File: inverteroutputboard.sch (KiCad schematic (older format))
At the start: 111 parts, among them P1 B+, P2 finishwinding, P3 B+, P4 startwinding, P5 CONN_02X05, Q1 Q_NMOS_GDS, Q10 Q_NMOS_GDS, Q11 Q_NMOS_GDS, Q12 Q_NMOS_GDS, Q13 Q_NMOS_GDS, Q14 Q_NMOS_GDS, Q15 Q_NMOS_GDS, Q16 Q_NMOS_GDS, Q17 Q_NMOS_GDS, Q18 Q_NMOS_GDS, Q19 Q_NMOS_GDS, Q2 Q_NMOS_GDS, Q20 Q_NMOS_GDS, Q21 Q_NMOS_GDS, Q22 Q_NMOS_GDS, Q23 Q_NMOS_GDS, Q24 Q_NMOS_GDS, Q3 Q_NMOS_GDS, Q4 Q_NMOS_GDS, Q5 Q_NMOS_GDS, Q6 Q_NMOS_GDS, Q7 Q_NMOS_GDS, Q8 Q_NMOS_GDS, Q9 Q_NMOS_GDS

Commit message: added jumbpers
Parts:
- removed C2, C4, C5: 104/100v, Capacitors_ThroughHole:C_Disc_D7.5_P5, symbol C
- removed C3, C6: 472/1kv, Capacitors_ThroughHole:C_Disc_D12_P7.75, symbol C
- removed D10, D11, D12, D13, D14, D15, D16, D17, D19, D20, D21, D22, D23, D24, D7, D8, D9: 1N5819, Diodes_SMD:DO-214AB_Handsoldering, symbol D_Schottky_Small
- removed D18: D_Schottky_Small, Diodes_SMD:DO-214AB_Handsoldering, symbol D_Schottky_Small
- removed P2: finishwinding, Connect:1pin, symbol CONN_01X01
- removed P3: B+, Connect:1pin, symbol CONN_01X01
- removed P4: startwinding, Connect:1pin, symbol CONN_01X01
- removed Q10, Q11, Q12, Q13, Q14, Q15, Q16, Q17, Q18, Q19, Q20, Q21, Q22, Q23, Q24, Q7, Q8, Q9: Q_NMOS_GDS, TO_SOT_Packages_THT:TO-220_Neutral123_Horizontal_MountedFromLS_LargePads, symbol Q_NMOS_GDS
- removed R14, R27, R40: 47R1/2w, Resistors_ThroughHole:Resistor_Horizontal_RM10mm, symbol R
- removed R15, R16, R18, R19, R20, R21, R28, R29, R31, R32, R33, R34, R41, R42, R44, R45, R46, R47: 20k, Resistors_SMD:R_0603_HandSoldering, symbol R
- removed R17, R22, R23, R24, R25, R26, R30, R35, R36, R37, R38, R39, R43, R48, R49, R50, R51, R52: 5.6, Resistors_SMD:R_0603_HandSoldering, symbol R
- added JP?: pwm-c, symbol JUMPER
- added JP?: pwm-d, symbol JUMPER
- added JP?: pwm-b, symbol JUMPER
- added JP?: pwm-a, symbol JUMPER
- added JP?: endwind, symbol JUMPER
- added JP?: startwind, symbol JUMPER
- added JP?: gnd, symbol JUMPER
- added JP?: b+, symbol JUMPER
- added P?: CONN_02X05, Connect:IDC_Header_Straight_10pins, symbol CONN_02X05
- Q1, Q2, Q3, Q4, Q5, Q6: footprint TO_SOT_Packages_THT:TO-220_Neutral123_Horizontal_MountedFromLS_LargePads -> TO_SOT_Packages_THT:TO-220_Neutral123_Vertical
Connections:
- net B+: now also JP?.1, JP?.2, P?.10 (P10), P?.9 (P9)
- net GND: now also JP?.1, P?.1 (P1), P?.2 (P2)
- net PWM-A: now also JP?.1, P?.3 (P3)
- net PWM-B: now also JP?.1, P?.7 (P7)
- net PWM-C: now also D3.1 (K), JP?.1, JP?.2, JP?.2, JP?.2, JP?.2, P?.4 (P4)
- net PWM-D: now also JP?.1, P?.8 (P8)
- net endwinding: now also JP?.1, JP?.2, JP?.2, JP?.2, P?.6 (P6)
- net startwinding: now also JP?.1, P?.5 (P5)
- net at Q4.1 (G), R12.1, R8.1: now also D3.2 (A)
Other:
- moved on the sheet: P5

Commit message: version 0.9 caps and connectors
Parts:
- removed P1: B+, Connect:1pin, symbol CONN_01X01
- added C2, C3: CP, Capacitors_ThroughHole:C_Radial_D35_L51_P10, symbol CP
- JP1, JP2, JP3, JP4, JP5, JP6, JP7, JP8: renamed from JP?; footprint (none) -> Connectors_JST:JST_EH_B02B-EH-A_02x2.50mm_Straight
- gave numbers to parts that had none: 1
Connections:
- net B+: no longer C1.2, JP1.2, Q1.2 (D), Q2.2 (D), Q3.2 (D), Q4.2 (D), Q5.2 (D), Q6.2 (D)
- net PWM-C: no longer D1.1 (K), D2.1 (K), D3.1 (K), D4.1 (K), D5.1 (K), D6.1 (K), JP2.2, JP3.2, JP4.2, JP5.2, R10.2, R11.2, R12.2, R13.2, R4.2, R9.2
- net endwinding: no longer JP6.2, JP7.2, JP8.2, Q1.3 (S), Q2.3 (S), Q3.3 (S), Q4.3 (S), Q5.3 (S), Q6.3 (S), R1.2, R2.2, R3.2, R5.2, R6.2, R7.2, R8.2
- new net: C1.2, JP1.2, Q1.2 (D), Q2.2 (D), Q3.2 (D), Q4.2 (D), Q5.2 (D), Q6.2 (D)
- new net: JP6.2, JP7.2, JP8.2, Q1.3 (S), Q2.3 (S), Q3.3 (S), Q4.3 (S), Q5.3 (S), Q6.3 (S), R1.2, R2.2, R3.2, R5.2, R6.2, R7.2, R8.2
- new net: D1.1 (K), D2.1 (K), D3.1 (K), D4.1 (K), D5.1 (K), D6.1 (K), JP2.2, JP3.2, JP4.2, JP5.2, R10.2, R11.2, R12.2, R13.2, R4.2, R9.2
- new net: C2.1, C3.1
- new net: C2.2, C3.2
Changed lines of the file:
@@
 	7950 1500 7950 1475
 Connection ~ 4200 1750
-$Comp
-L CONN_01X01 P1
-U 1 1 57CCC886
-P 3175 1075
-F 0 "P1" H 3175 1175 50  0000 C CNN
-F 1 "B+" V 3275 1075 50  0000 C CNN
-F 2 "Connect:1pin" H 3175 1075 50  0001 C CNN
-F 3 "" H 3175 1075 50  0000 C CNN
-	1    3175 1075
-	-1   0    0    1
-$EndComp
 Wire Wire Line
 	3375 1075 4250 1075
@@
 	4250 1075 4250 1150
 Connection ~ 4250 1150
-Text Label 3175 1875 0    60   ~ 0
-PWM-C
 Wire Wire Line
 	3175 1875 3600 1875
 Connection ~ 3600 1875
-Text Label 3725 975  0    60   ~ 0
-B+
 Wire Wire Line
 	3725 975  3725 1075
@@
 	7475 1850 7475 1900
 Connection ~ 7475 1900
-Text Label 4000 1750 0    60   ~ 0
-endwinding
 Wire Wire Line
 	5375 1650 5375 1525
@@
 Connection ~ 5375 1900
 $Comp
-L CONN_02X05 P?
+L CONN_02X05 P2
 U 1 1 58034A1E
 P 2300 4975
-F 0 "P?" H 2300 5275 50  0000 C CNN
+F 0 "P2" H 2300 5275 50  0000 C CNN
 F 1 "CONN_02X05" H 2300 4675 50  0000 C CNN
 F 2 "Connect:IDC_Header_Straight_10pins" H 2300 3775 50  0001 C CNN
@@
 Connection ~ 2275 4575
 $Comp
-L GND #PWR?
+L GND #PWR02
 U 1 1 58034A2B
 P 2300 5425
-F 0 "#PWR?" H 2300 5175 50  0001 C CNN
+F 0 "#PWR02" H 2300 5175 50  0001 C CNN
 F 1 "GND" H 2300 5275 50  0000 C CNN
 F 2 "" H 2300 5425 50  0000 C CNN
@@
 	1950 4875 2050 4875
 $Comp
-L JUMPER JP?
+L JUMPER JP5
 U 1 1 58034C90
 P 2850 1875
-F 0 "JP?" H 2850 2025 50  0000 C CNN
+F 0 "JP5" H 2850 2025 50  0000 C CNN
 F 1 "pwm-c" H 2850 1795 50  0000 C CNN
-F 2 "" H 2850 1875 50  0000 C CNN
+F 2 "Connectors_JST:JST_EH_B02B-EH-A_02x2.50mm_Straight" H 2850 1875 50  0001 C CNN
 F 3 "" H 2850 1875 50  0000 C CNN
 	1    2850 1875
@@
 $EndComp
 $Comp
-L JUMPER JP?
+L JUMPER JP3
 U 1 1 58034D23
 P 2825 1625
-F 0 "JP?" H 2825 1775 50  0000 C CNN
+F 0 "JP3" H 2825 1775 50  0000 C CNN
 F 1 "pwm-d" H 2825 1545 50  0000 C CNN
-F 2 "" H 2825 1625 50  0000 C CNN
+F 2 "Connectors_JST:JST_EH_B02B-EH-A_02x2.50mm_Straight" H 2825 1625 50  0001 C CNN
 F 3 "" H 2825 1625 50  0000 C CNN
 	1    2825 1625
@@
 $EndComp
 $Comp
-L JUMPER JP?
+L JUMPER JP2
 U 1 1 58034DAC
 P 2825 1350
-F 0 "JP?" H 2825 1500 50  0000 C CNN
+F 0 "JP2" H 2825 1500 50  0000 C CNN
 F 1 "pwm-b" H 2825 1270 50  0000 C CNN
-F 2 "" H 2825 1350 50  0000 C CNN
+F 2 "Connectors_JST:JST_EH_B02B-EH-A_02x2.50mm_Straight" H 2825 1350 50  0001 C CNN
 F 3 "" H 2825 1350 50  0000 C CNN
 	1    2825 1350
@@
 $EndComp
 $Comp
-L JUMPER JP?
+L JUMPER JP4
 U 1 1 58034E3E
 P 2825 2075
-F 0 "JP?" H 2825 2225 50  0000 C CNN
+F 0 "JP4" H 2825 2225 50  0000 C CNN
 F 1 "pwm-a" H 2825 1995 50  0000 C CNN
-F 2 "" H 2825 2075 50  0000 C CNN
+F 2 "Connectors_JST:JST_EH_B02B-EH-A_02x2.50mm_Straight" H 2825 2075 50  0001 C CNN
 F 3 "" H 2825 2075 50  0000 C CNN
 	1    2825 2075
@@
 	2525 2025 2525 2075
 $Comp
-L JUMPER JP?
+L JUMPER JP7
 U 1 1 58035E03
 P 4100 2250
-F 0 "JP?" H 4100 2400 50  0000 C CNN
+F 0 "JP7" H 4100 2400 50  0000 C CNN
 F 1 "endwind" H 4100 2170 50  0000 C CNN
-F 2 "" H 4100 2250 50  0000 C CNN
+F 2 "Connectors_JST:JST_EH_B02B-EH-A_02x2.50mm_Straight" H 4100 2250 50  0001 C CNN
 F 3 "" H 4100 2250 50  0000 C CNN
 	1    4100 2250
@@
 Connection ~ 4400 1750
 $Comp
-L JUMPER JP?
+L JUMPER JP6
 U 1 1 58035F8A
 P 4075 2500
-F 0 "JP?" H 4075 2650 50  0000 C CNN
+F 0 "JP6" H 4075 2650 50  0000 C CNN
 F 1 "startwind" H 4075 2420 50  0000 C CNN
-F 2 "" H 4075 2500 50  0000 C CNN
+F 2 "Connectors_JST:JST_EH_B02B-EH-A_02x2.50mm_Straight" H 4075 2500 50  0001 C CNN
 F 3 "" H 4075 2500 50  0000 C CNN
 	1    4075 2500
@@
 Connection ~ 2800 2775
 $Comp
-L JUMPER JP?
+L JUMPER JP8
 U 1 1 580368FD
 P 4100 2950
-F 0 "JP?" H 4100 3100 50  0000 C CNN
+F 0 "JP8" H 4100 3100 50  0000 C CNN
 F 1 "gnd" H 4100 2870 50  0000 C CNN
-F 2 "" H 4100 2950 50  0000 C CNN
+F 2 "Connectors_JST:JST_EH_B02B-EH-A_02x2.50mm_Straight" H 4100 2950 50  0001 C CNN
 F 3 "" H 4100 2950 50  0000 C CNN
 	1    4100 2950
@@
 Connection ~ 2625 3050
 $Comp
-L JUMPER JP?
+L JUMPER JP1
 U 1 1 58037102
 P 2725 800
-F 0 "JP?" H 2725 950 50  0000 C CNN
+F 0 "JP1" H 2725 950 50  0000 C CNN
 F 1 "b+" H 2725 720 50  0000 C CNN
-F 2 "" H 2725 800 50  0000 C CNN
+F 2 "Connectors_JST:JST_EH_B02B-EH-A_02x2.50mm_Straight" H 2725 800 50  0001 C CNN
 F 3 "" H 2725 800 50  0000 C CNN
 	1    2725 800
@@
 Wire Wire Line
 	2425 700  2425 800
+Connection ~ 3175 1875
+$Comp
+L CP C2
+U 1 1 5803BE58
+P 5225 3850
+F 0 "C2" H 5250 3950 50  0000 L CNN
+F 1 "CP" H 5250 3750 50  0000 L CNN
+F 2 "Capacitors_ThroughHole:C_Radial_D35_L51_P10" H 5263 3700 50  0001 C CNN
+F 3 "" H 5225 3850 50  0000 C CNN
+	1    5225 3850
+	1    0    0    -1
+$EndComp
+$Comp
+L CP C3
+U 1 1 5803BF11
+P 5600 3875
+F 0 "C3" H 5625 3975 50  0000 L CNN
+F 1 "CP" H 5625 3775 50  0000 L CNN
+F 2 "Capacitors_ThroughHole:C_Radial_D35_L51_P10" H 5638 3725 50  0001 C CNN
+F 3 "" H 5600 3875 50  0000 C CNN
+	1    5600 3875
+	1    0    0    -1
+$EndComp
+Wire Wire Line
+	5225 3700 5600 3700
+Wire Wire Line
+	5600 3700 5600 3725
+Wire Wire Line
+	5600 4025 5225 4025
+Wire Wire Line
+	5225 4025 5225 4000
 $EndSCHEMATC

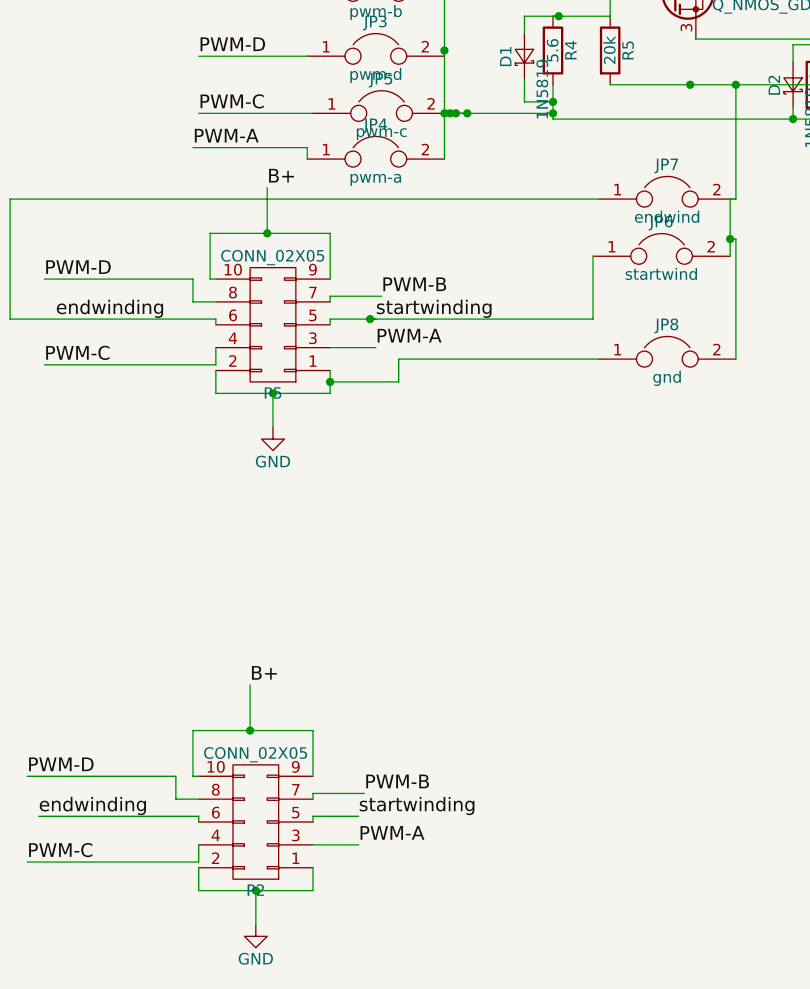
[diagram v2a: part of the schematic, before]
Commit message: reworked plugs to make compatible with powerstar inverters and added better solder masking.
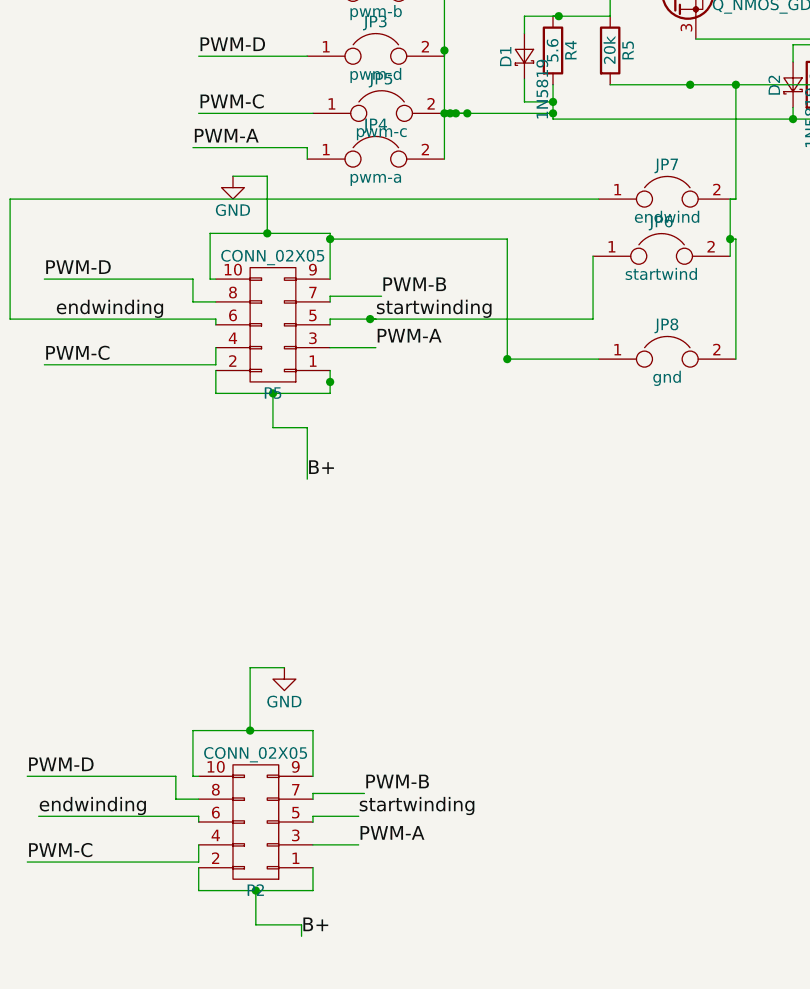
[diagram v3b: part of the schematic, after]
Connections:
- net B+: now also P2.1 (P1), P2.2 (P2), P5.1 (P1), P5.2 (P2); no longer P2.10 (P10), P2.9 (P9), P5.10 (P10), P5.9 (P9)
- net GND: now also P2.10 (P10), P2.9 (P9), P5.10 (P10), P5.9 (P9); no longer P2.1 (P1), P2.2 (P2), P5.1 (P1), P5.2 (P2)
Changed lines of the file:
@@
 Wire Wire Line
 	2625 2400 2625 2600
-Text Label 2350 2200 0    60   ~ 0
+Text Label 2525 3475 0    60   ~ 0
 B+
 Wire Wire Line
-	2350 2200 2350 2400
+	2350 2150 2350 2400
 Connection ~ 2350 2400
 $Comp
 L GND #PWR01
 U 1 1 57CD0DDC
-P 2375 3250
-F 0 "#PWR01" H 2375 3000 50  0001 C CNN
-F 1 "GND" H 2375 3100 50  0000 C CNN
-F 2 "" H 2375 3250 50  0000 C CNN
-F 3 "" H 2375 3250 50  0000 C CNN
-	1    2375 3250
+P 2200 2150
+F 0 "#PWR01" H 2200 1900 50  0001 C CNN
+F 1 "GND" H 2200 2000 50  0000 C CNN
+F 2 "" H 2200 2150 50  0000 C CNN
+F 3 "" H 2200 2150 50  0000 C CNN
+	1    2200 2150
 	1    0    0    -1
 $EndComp
@@
 Wire Wire Line
 	2550 4575 2550 4775
-Text Label 2275 4375 0    60   ~ 0
+Text Label 2500 5475 0    60   ~ 0
 B+
 Wire Wire Line
-	2275 4375 2275 4575
+	2275 4300 2275 4575
 Connection ~ 2275 4575
 $Comp
 L GND #PWR02
 U 1 1 58034A2B
-P 2300 5425
-F 0 "#PWR02" H 2300 5175 50  0001 C CNN
-F 1 "GND" H 2300 5275 50  0000 C CNN
-F 2 "" H 2300 5425 50  0000 C CNN
-F 3 "" H 2300 5425 50  0000 C CNN
-	1    2300 5425
+P 2425 4300
+F 0 "#PWR02" H 2425 4050 50  0001 C CNN
+F 1 "GND" H 2425 4150 50  0000 C CNN
+F 2 "" H 2425 4300 50  0000 C CNN
+F 3 "" H 2425 4300 50  0000 C CNN
+	1    2425 4300
 	1    0    0    -1
 $EndComp
@@
 	4400 2425 4375 2425
 Connection ~ 4375 2425
-Wire Wire Line
-	3800 2950 2925 2950
-Wire Wire Line
-	2925 2950 2925 3050
-Wire Wire Line
-	2925 3050 2625 3050
 Connection ~ 2625 3050
 $Comp
@@
 Wire Wire Line
 	5225 4025 5225 4000
+Wire Wire Line
+	2275 4300 2425 4300
+Wire Wire Line
+	2300 5425 2500 5425
+Wire Wire Line
+	2500 5425 2500 5475
+Wire Wire Line
+	2200 2150 2350 2150
+Wire Wire Line
+	2375 3250 2525 3250
+Wire Wire Line
+	2525 3250 2525 3475
+Wire Wire Line
+	2625 2425 3400 2425
+Wire Wire Line
+	3400 2425 3400 2950
+Connection ~ 3400 2950
+Connection ~ 2625 2425
+Wire Wire Line
+	3400 2950 3800 2950
 $EndSCHEMATC
